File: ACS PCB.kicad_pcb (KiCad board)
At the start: 4 copper layers, 72.4 x 72.4 mm, 72 parts, among them J1 Conn_01x02, J3 Conn_01x01, J5 Conn_01x02, Q1 2SC1815, U1 LSM6DSV80XTR, U3 LSM6DSV80XTR, U4 BMP581, U5 BMP581, U6 BMP581, U7 LSM6DSV80XTR, U8 PLM62440APPQRJRTQ1

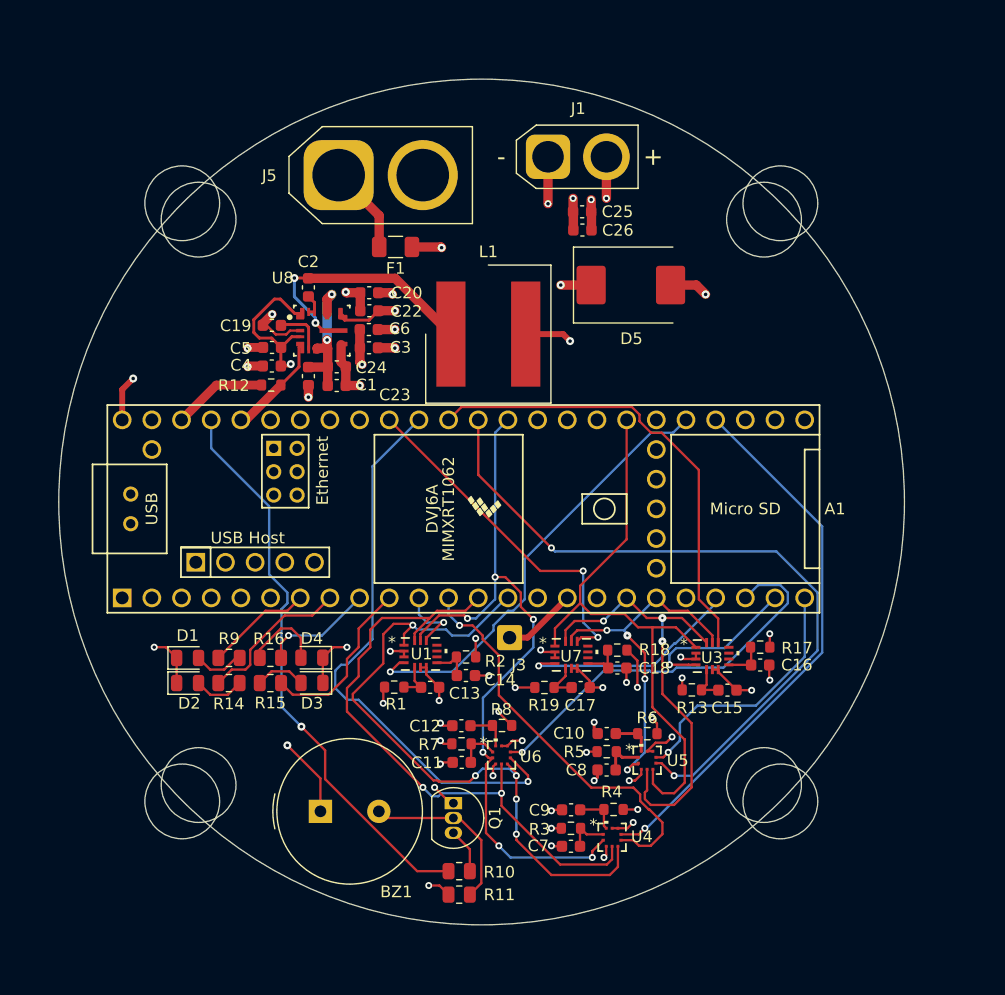
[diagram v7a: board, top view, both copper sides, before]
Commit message: Fixed capacitor placement
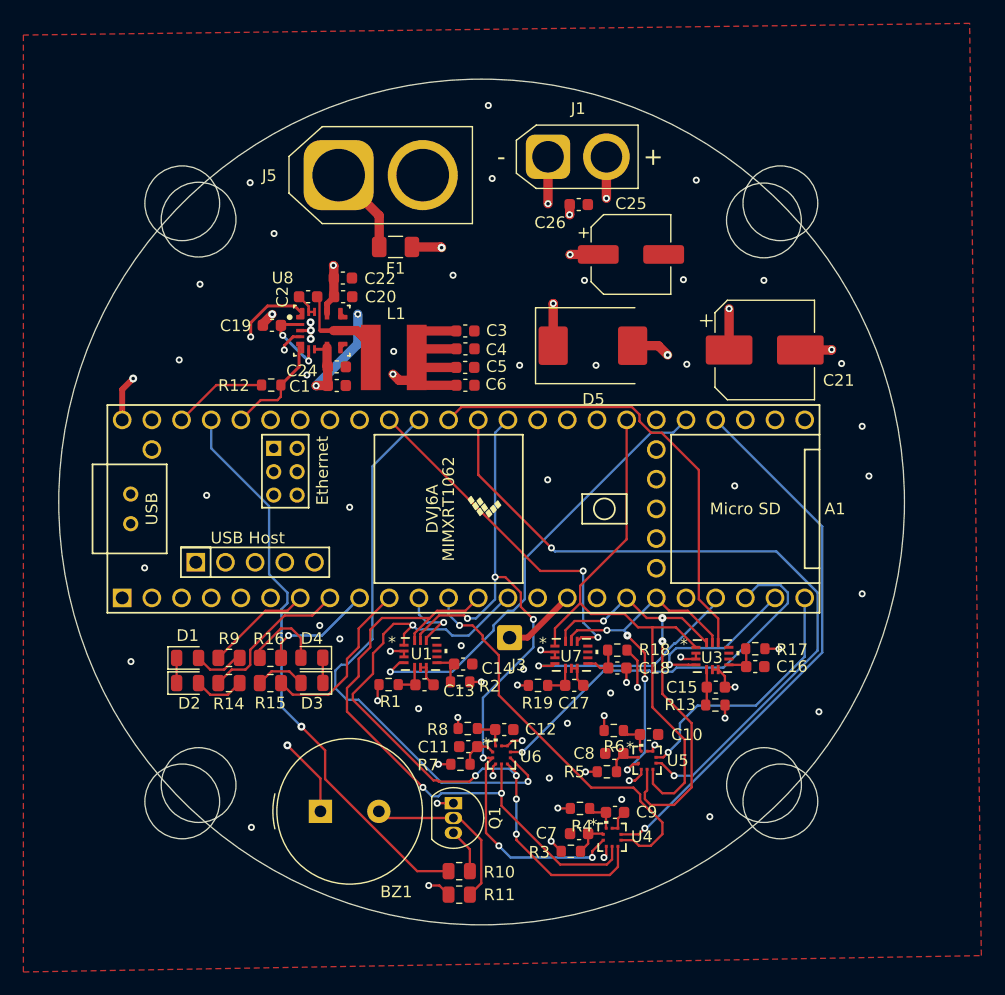
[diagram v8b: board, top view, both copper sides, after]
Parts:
- removed C23: 100uF, Capacitor_SMD:C_0603_1608Metric
- removed REF**: MountingHole_6.4mm_M6, MountingHole:MountingHole_6.4mm_M6
- added ?: , , F.Cu at (172.2, 63.5)
- added C21: 100uF, Capacitor_SMD:CP_Elec_8x6.7, F.Cu at (172.3, 74.6)
- C25: footprint Capacitor_SMD:C_0603_1608Metric -> Capacitor_SMD:CP_Elec_6.3x9.9
- L1: value 1090_78439369047 -> 5030_7443845030120; footprint Inductor78439358047:L_Wurth_WE-XHMA-1090 -> BMP581:wurst7443845030120
- moved C4 16.6 mm to (146.6, 74.5), turned to 0 degrees
- moved C5 16.6 mm to (146.6, 76.0), turned to 0 degrees
- moved C6 9.54 mm to (146.6, 77.6)
- moved C3 8.36 mm to (146.6, 72.9)
- moved L1 7.15 mm to (143.3, 78.0), turned to 180 degrees
- moved D5 6.12 mm to (157.6, 74.2)
- moved C25 5.55 mm to (160.8, 66.4)
- moved C9 3.77 mm to (159.4, 114.1), turned to 180 degrees
- moved C12 3.68 mm to (150.0, 107.0), turned to 180 degrees
- moved C10 3.63 mm to (162.4, 107.5), turned to 180 degrees
- moved C22 3.60 mm to (136.2, 68.4)
- moved R8 2.95 mm to (146.8, 107.0), turned to 180 degrees
- moved R6 2.89 mm to (159.3, 107.1), turned to 180 degrees
- moved R4 2.88 mm to (156.4, 113.8), turned to 180 degrees
- moved R13 2.39 mm to (168.0, 105.0), turned to 180 degrees
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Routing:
- net GND: track 82.8 -> 43.4 mm, vias 36 -> 56
- net +5V: track 24.9 -> 36.2 mm
- net Net-(U8-SW): track 21.8 -> 10.9 mm, vias 2 -> 0
- net +BATT: track 27.1 -> 34.4 mm, vias 7 -> 9
- net Net-(U8-MODE_SYNC): track 4.38 -> 6.72 mm, vias 0 -> 2
- net +3.3V: track 34.7 -> 32.8 mm
- net Net-(U4-VDD): track 3.74 -> 2.91 mm
- net Net-(U6-VDD): track 3.75 -> 2.98 mm
- net Net-(U4-VDDIO): track 3.71 -> 3.10 mm
- net VoltMonitor: track 8.85 -> 9.43 mm
- net Net-(U7-VDDIO): track 3.55 -> 2.97 mm
- added copper zone on F.Cu, net GND
